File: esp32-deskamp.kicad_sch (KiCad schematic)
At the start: 29 parts, among them J1 INPUT 00, J10 ADDITIONAL GPIO, J2 INPUT 01, J3 MUTE, J4 SLEEP, J5 PRE OUT, J6 LFE OUT, J7 INPUT SELECT, J8 MOTOR, J9 12V IN, K1 INPUT 00, K2 INPUT 01, K3 AMP MUTE, K4 AMP SLEEP, U1 ESP32 D1 MINI, U2 TSR 1-2433, U3 L9110, U4 ULN2003A

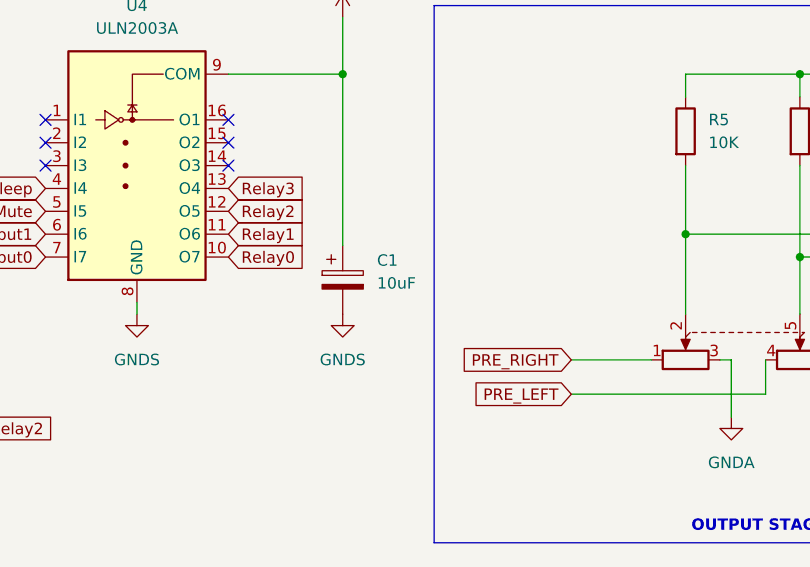
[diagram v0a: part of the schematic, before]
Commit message: Change to proper µ symbol
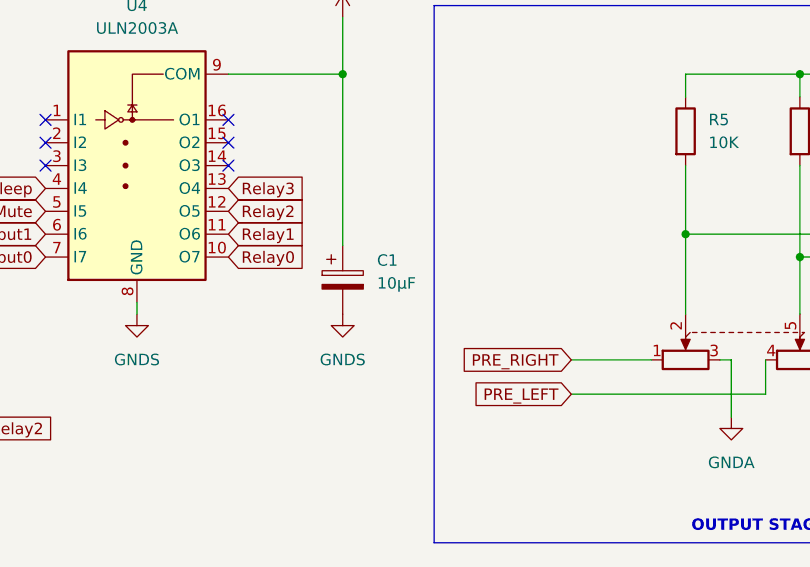
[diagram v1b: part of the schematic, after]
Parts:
- C1: value 10uF -> 10µF
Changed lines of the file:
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@@
 			)
 		)
-		(property "Value" "10uF"
+		(property "Value" "10µF"
 			(at 137.16 117.2209 0)
 			(effects
